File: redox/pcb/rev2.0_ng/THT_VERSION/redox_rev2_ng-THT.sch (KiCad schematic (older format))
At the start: 147 parts, among them J2 OLED-SSD1306, K1 KEYSW, K10 KEYSW, K11 KEYSW, K12 KEYSW, K13 KEYSW, K14 KEYSW, K15 KEYSW, K16 KEYSW, K17 KEYSW, K18 KEYSW, K19 KEYSW, K2 KEYSW, K20 KEYSW, K21 KEYSW, K22 KEYSW, K23 KEYSW, K24 KEYSW, K25 KEYSW, K26 KEYSW, K27 KEYSW, K28 KEYSW, K29 KEYSW, K3 KEYSW, K30 KEYSW, K31 KEYSW, K32 KEYSW, K33 KEYSW, K34 KEYSW, K35 KEYSW, K4 KEYSW, K5 KEYSW, K6 KEYSW, K7 KEYSW, K8 KEYSW, K9 KEYSW, P1 TC2030-AVR, Q1 2N7002, U1 PRTR5V0U2X, U2 ATmega32U4, Y1 16Mhz

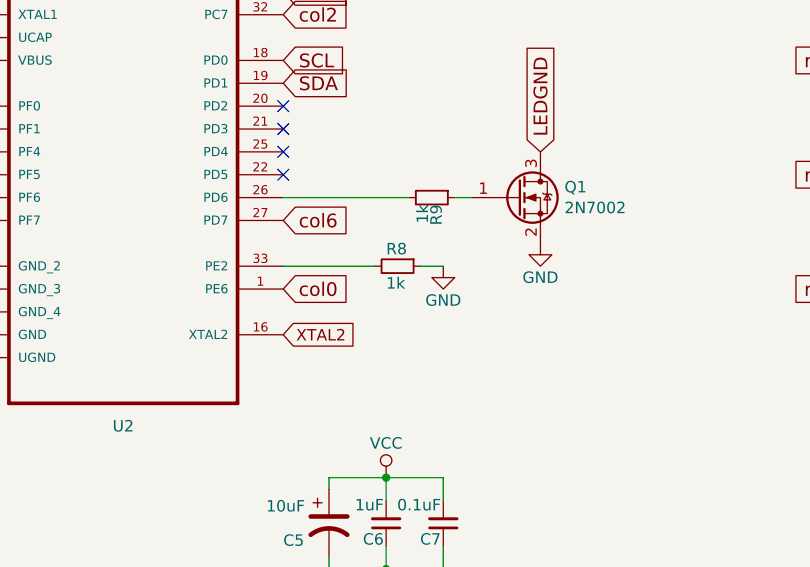
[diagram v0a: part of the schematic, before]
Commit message: Change PCB holes placement, TRSS connector, add JLC id.
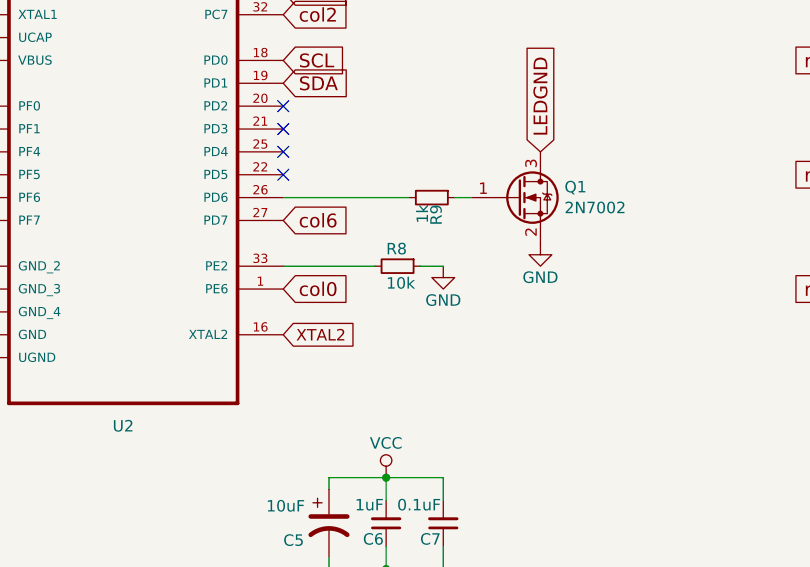
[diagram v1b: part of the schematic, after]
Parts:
- H1, H2, H3, H4: footprint redox_footprints:HOLE_M3 -> redox_footprints:HOLE_M2_TH
- R8: value 1k -> 10k
- TRRS1: footprint Keebio-Parts:TRRS-PJ-320A-dual -> redox_footprints:MJ-4PP-9
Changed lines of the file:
@@
 F 0 "TRRS1" H 3000 6780 50  0000 C CNN
 F 1 "Audio-Jack-4" H 3170 6330 50  0000 C CNN
-F 2 "Keebio-Parts:TRRS-PJ-320A-dual" H 3300 6800 50  0001 C CNN
+F 2 "redox_footprints:MJ-4PP-9" H 3300 6800 50  0001 C CNN
 F 3 "" H 3300 6800 50  0001 C CNN
 	1    3050 6700
@@
 AR Path="/5EDAEC91" Ref="R8"  Part="1"
 F 0 "R8" V 4600 3175 50  0000 L CNN
-F 1 "1k" V 4750 3175 50  0000 L CNN
+F 1 "10k" V 4750 3175 50  0000 L CNN
 F 2 "Keebio-Parts:R_0603" H 4675 3225 50  0001 C CNN
 F 3 "" H 4675 3225 50  0001 C CNN
@@
 F 0 "H1" H 3350 7596 50  0000 L CNN
 F 1 "MountingHole" H 3000 7725 50  0000 L CNN
-F 2 "redox_footprints:HOLE_M3" H 3250 7550 50  0001 C CNN
+F 2 "redox_footprints:HOLE_M2_TH" H 3250 7550 50  0001 C CNN
 F 3 "~" H 3250 7550 50  0001 C CNN
 	1    3250 7550
@@
 F 0 "H2" H 3575 7500 50  0000 L CNN
 F 1 "MountingHole" H 3525 7375 50  0000 L CNN
-F 2 "redox_footprints:HOLE_M3" H 3775 7550 50  0001 C CNN
+F 2 "redox_footprints:HOLE_M2_TH" H 3775 7550 50  0001 C CNN
 F 3 "~" H 3775 7550 50  0001 C CNN
 	1    3775 7550
@@
 F 0 "H3" H 4400 7596 50  0000 L CNN
 F 1 "MountingHole" H 4050 7725 50  0000 L CNN
-F 2 "redox_footprints:HOLE_M3" H 4300 7550 50  0001 C CNN
+F 2 "redox_footprints:HOLE_M2_TH" H 4300 7550 50  0001 C CNN
 F 3 "~" H 4300 7550 50  0001 C CNN
 	1    4300 7550
@@
 F 0 "H4" H 4925 7596 50  0000 L CNN
 F 1 "MountingHole" H 4575 7725 50  0000 L CNN
-F 2 "redox_footprints:HOLE_M3" H 4825 7550 50  0001 C CNN
+F 2 "redox_footprints:HOLE_M2_TH" H 4825 7550 50  0001 C CNN
 F 3 "~" H 4825 7550 50  0001 C CNN
 	1    4825 7550
